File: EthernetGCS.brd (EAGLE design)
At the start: 45.7 x 16.8 mm, 19 parts, among them U1 MIC5219-3.3V, U3 FT232RL-BASICSSOP, X1 USB-A-H

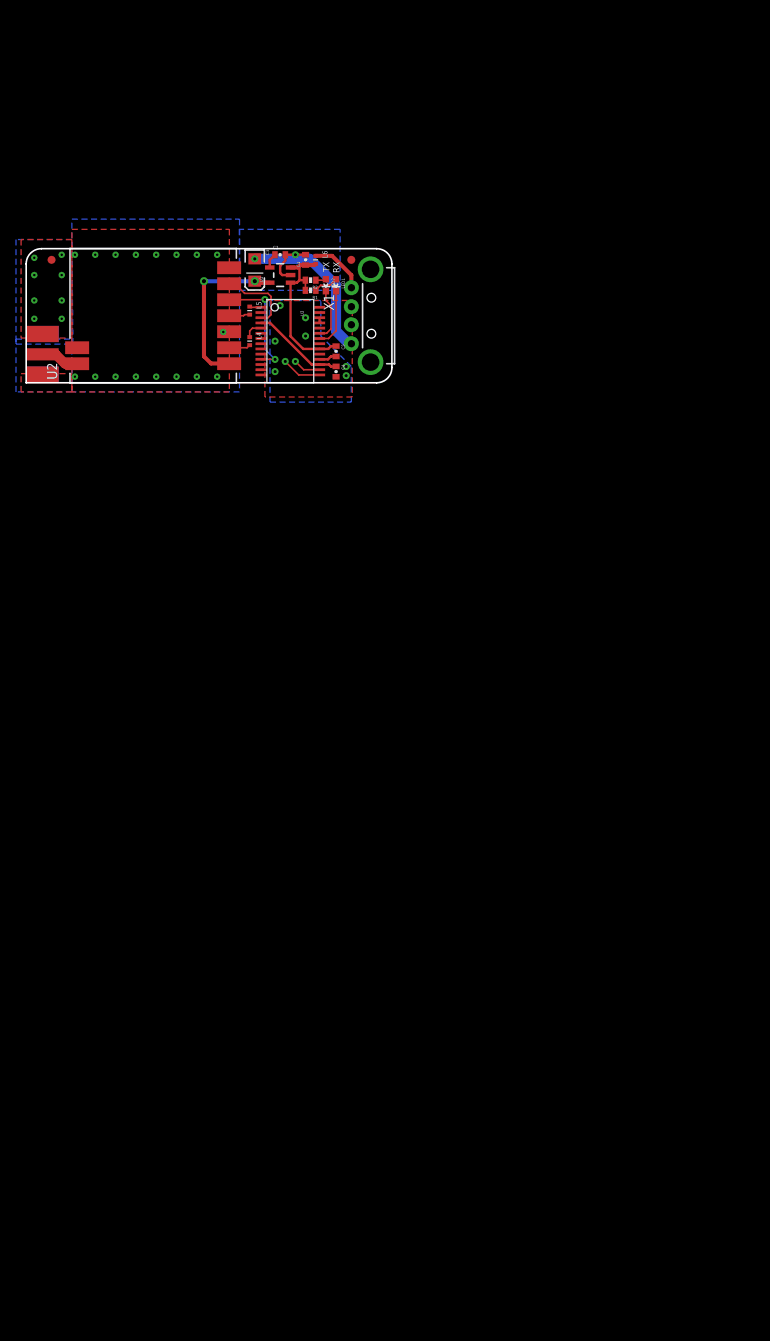
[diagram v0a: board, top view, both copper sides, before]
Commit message: Adding Ethernet IC, a PIC 24F and a RJ45 connector.
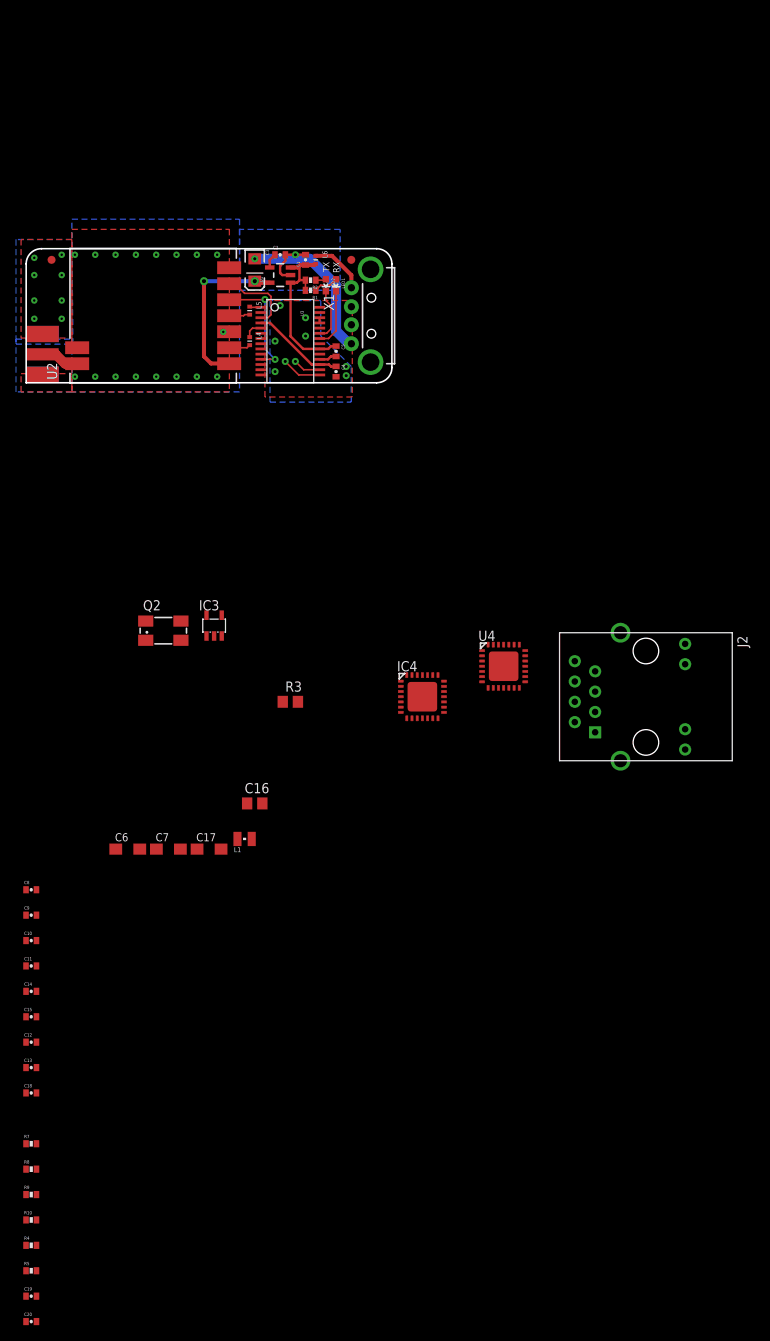
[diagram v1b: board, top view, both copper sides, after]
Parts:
- added C10, C11, C12, C13, C14, C15, C18, C8, C9: 0.1uF, SparkFun:0402-CAP
- added C16: 0.1uF, rcl:C0805
- added C17, C6, C7: 10uF, rcl:SMC_A
- added C19, C20: 27pf, SparkFun:0402-CAP
- added IC3: 24AA00OT, microchip:SOT23-5L
- added IC4: PIC24FJ64GA002_QFN, microchip:QFN28-ML_6X6MM
- added J2: HR911105A, CONNECTER:HR911105A
- added L1: (no value), wuerth-elektronik:WE-KI_0805_B
- added Q2: 25Mhz, crystal:CTS406
- added R10, R7, R8, R9: 49R9 1%, SparkFun:0402-RES
- added R3: 2K32, rcl:R0805
- added R4, R5: 330, SparkFun:0402-RES
- added U4: ENC28J60-QFN, microchip-enc28j60:QFN28
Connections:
- new net CCT: C15.1, J2.4, L1.2, R10.2, R9.2
- new net ETH-CLK: U4.4
- new net ETH-CS: U4.5
- new net ETH-INT: U4.28
- new net ETH-MISO: U4.2
- new net ETH-MOSI: U4.3
- new net ETH-RST: U4.6
- new net LED_LINK: J2.9, R5.2
- new net LED_STATUS: J2.12, R4.2
- new net N$13: C6.+, U4.25
- new net N$14: C19.1, Q2.1, U4.20
- new net N$15: C20.1, Q2.3, U4.19
- new net N$16: C7.+
- new net N$17: R3.2, U4.10
- new net N$18: R5.1, U4.23
- new net N$19: R4.1, U4.22
- new net N$22: C14.2, R7.2, R8.2
- new net RD+: J2.3, R8.1, U4.9
- new net RD-: J2.6, R7.1, U4.8
- new net SCL_1: IC3.1
- new net SDA_1: IC3.3
- new net TD+: J2.1, R10.1, U4.13
- new net TD-: J2.2, R9.1, U4.12
- new net V+: C10.1, C11.1, C12.1, C13.1, C16.1, C17.+, C18.1, C8.1, C9.1, IC3.4, L1.1, U4.11, U4.15, U4.16, U4.21, U4.24
- new net VDD: IC4.10, IC4.25
- new net VDDCORE: IC4.17
- new net VSS: IC4.24, IC4.5
- net GND: now also C10.2, C11.2, C12.2, C13.2, C14.1, C15.2, C16.2, C17.-, C18.2, C19.2, C20.2, C6.-, C7.-, C8.2, C9.2, IC3.2, J2.10, J2.11, J2.13, J2.14, R3.1, U4.14, U4.17, U4.18, U4.26, U4.7, U4.EXP

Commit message: Cloning 3DR board, to use as reference.
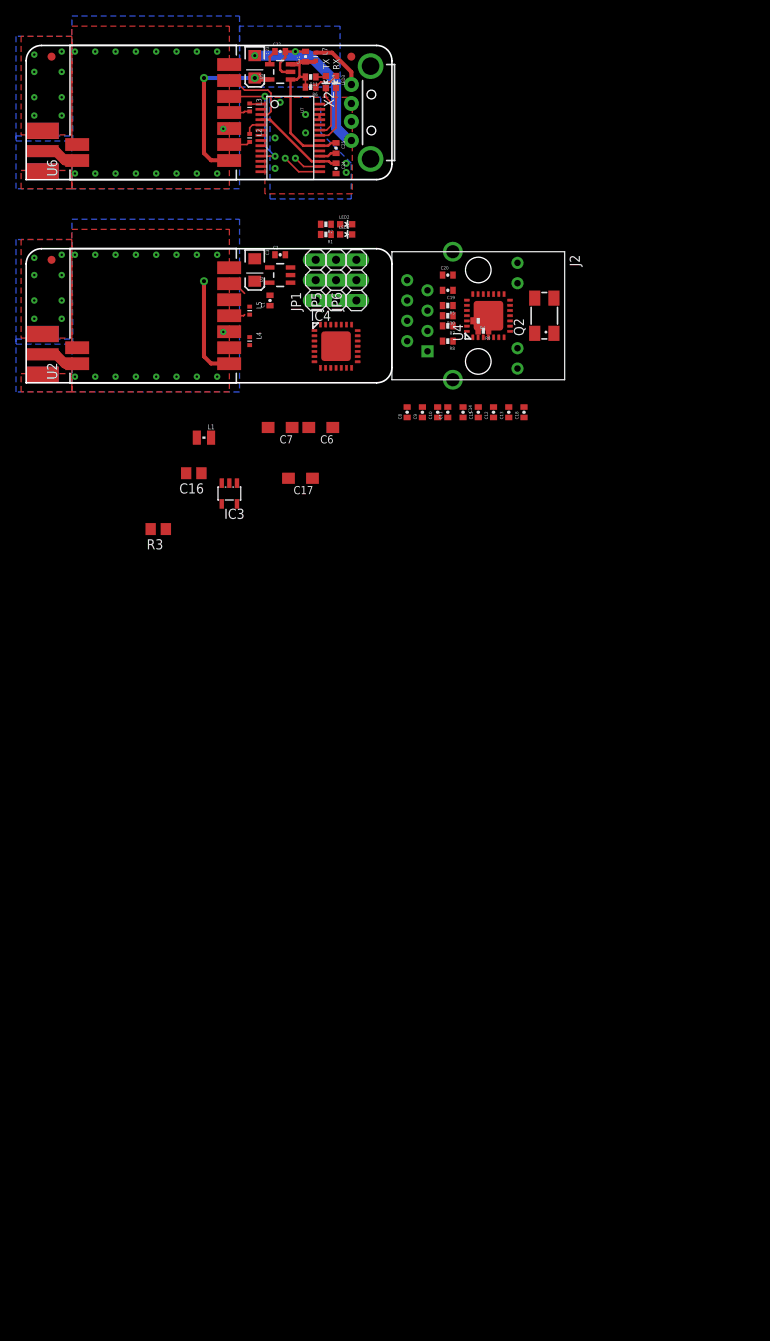
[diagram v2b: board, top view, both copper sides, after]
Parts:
- removed C4, C5: 0.1uF, SparkFun:0402-CAP
- removed L6: BKP1005HS121-T, pel_dipol_comp:0402-IND
- removed U3: FT232RL-BASICSSOP, SparkFun:SSOP28DB
- removed X1: USB-A-H, SparkFun:USB-A-H
- added C21: 1uF, SparkFun:0402-CAP
- added C22: 470pF, SparkFun:0402-CAP
- added C23: 10uF, SparkFun:EIA3216
- added C24, C25: 0.1uF, SparkFun:0402-CAP
- added J$2: SMA_EDGE, 3DRobotics:SMA-EDGE
- added JP3, JP4: FIDUCIAL1X2, SparkFun:FIDUCIAL-1X2
- added JP5, JP6: (no value), pinhead:1X03
- added L2, L3: BLM15HD102SN1, pel_dipol_comp:0402-IND
- added L7: BKP1005HS121-T, pel_dipol_comp:0402-IND
- added LED3: GREEN, SparkFun:LED-0603
- added LED4: RED, SparkFun:LED-0603
- added R11, R6: 330, SparkFun:0402-RES
- added U5: MIC5219-3.3V, SparkFun:SOT23-5
- added U6: (no value), 3DRobotics:HM-TRP-SMD
- added U7: FT232RL-BASICSSOP, SparkFun:SSOP28DB
- added X2: USB-A-H, SparkFun:USB-A-H
- JP1: value FIDUCIAL1X2 -> (none); device SparkFun:FIDUCIAL-1X2 -> pinhead:1X03
- moved C20 140.8 mm to (52.7, 14.0)
- moved C19 136.1 mm to (52.7, 12.1), turned to 180 degrees
- moved R5 131.4 mm to (52.7, 10.2), turned to 180 degrees
- moved R4 128.4 mm to (56.5, 8.26), turned to 180 degrees
- moved R10 124.4 mm to (52.7, 8.89), turned to 180 degrees
- moved R9 121.8 mm to (57.1, 6.99), turned to 180 degrees
- moved R8 115.9 mm to (52.7, 5.71), turned to 180 degrees
- moved R7 114.7 mm to (52.7, 7.62), turned to 180 degrees
- moved C18 105.0 mm to (62.2, -3.17), turned to 90 degrees
- moved C13 101.4 mm to (60.3, -3.17), turned to 90 degrees
- moved C12 97.7 mm to (58.4, -3.17), turned to 90 degrees
- moved C15 94.0 mm to (56.5, -3.17), turned to 90 degrees
- moved C14 90.3 mm to (54.6, -3.17), turned to 270 degrees
- moved C11 86.6 mm to (52.7, -3.17), turned to 90 degrees
- moved C10 83.3 mm to (51.4, -3.17), turned to 90 degrees
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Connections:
- removed net DTR: U3.2
- removed net N$12: L6.P$1, X1.VBUS
- removed net N$3: C4.1, U3.17, U3.4
- removed net N$5: U3.15, X1.D+
- removed net N$6: U3.16, X1.D-
- new net CTS1: U6.!CONFIG, U7.11
- new net DTR1: U7.2
- new net N$20: C22.1, U5.4
- new net N$21: J$2.SIG, U6.ANT
- new net N$23: C24.1, U7.17, U7.4
- new net N$24: U7.15, X2.D+
- new net N$25: U7.16, X2.D-
- new net N$26: LED4.A, R11.1
- new net N$27: LED3.A, R6.1
- new net N$28: LED4.C, U7.23
- new net N$29: LED3.C, U7.22
- new net N$30: L2.P$2, U6.DTX
- new net N$31: L3.P$2, U6.DRX
- new net N$32: L7.P$1, X2.VBUS
- new net RTS1: U6.!ENABLE, U7.3
- new net RX1: L3.P$1, U7.1
- new net TX1: L2.P$1, U7.5
- net 3.3V: now also C23.A, U5.5, U6.VCC
- net 5V: now also C21.1, C25.1, L7.P$2, R11.2, R6.2, U5.1, U5.3, U7.20; no longer C5.1, L6.P$2, U3.20
- net CTS: no longer U3.11
- net GND: now also C21.2, C22.2, C23.C, C24.2, C25.2, J$2.GND@0, J$2.GND@1, J$2.GND@2, J$2.GND@3, U5.2, U6.AGND, U6.GND, U7.18, U7.21, U7.25, U7.26, U7.7, X2.GND; no longer C4.2, C5.2, U3.18, U3.21, U3.25, U3.26, U3.7, X1.GND
- net N$10: no longer U3.23
- net N$11: no longer U3.22
- net RTS: no longer U3.3
- net RX: no longer U3.1
- net TX: no longer U3.5
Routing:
- net N$6: track 16.5 -> 0.00 mm, vias 1 -> 0
- net N$25: track 0.00 -> 16.5 mm, vias 0 -> 1
- net N$5: track 16.3 -> 0.00 mm, vias 1 -> 0
- net N$24: track 0.00 -> 16.3 mm, vias 0 -> 1
- net CTS1: track 0.00 -> 14.3 mm, vias 0 -> 2
- net CTS: track 14.3 -> 0.00 mm, vias 2 -> 0
- net 3.3V: track 21.2 -> 34.2 mm, vias 2 -> 3
- net N$3: track 11.6 -> 0.00 mm
- net N$23: track 0.00 -> 11.6 mm
- net RTS1: track 0.00 -> 9.57 mm
- net N$29: track 0.00 -> 7.42 mm
- net N$11: track 7.42 -> 0.00 mm
- net RTS: track 9.57 -> 2.43 mm
- net N$32: track 0.00 -> 7.03 mm
- net N$12: track 7.03 -> 0.00 mm
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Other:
- board size 45.7 x 16.8 mm -> 45.7 x 42.2 mm
